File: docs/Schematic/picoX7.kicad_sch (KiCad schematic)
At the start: 33 parts, among them J1 MIDI in, J2 Debug, J3 Stereo line out, J4 Debug, SW1 RST, U1 MCU arm Cortex-M0x2, U2 I2S DAC, U3 H11L1, U4 74HCT164, U6 D1X8K-14BL, U7 D1X8K-14BL, U8 74HCT164

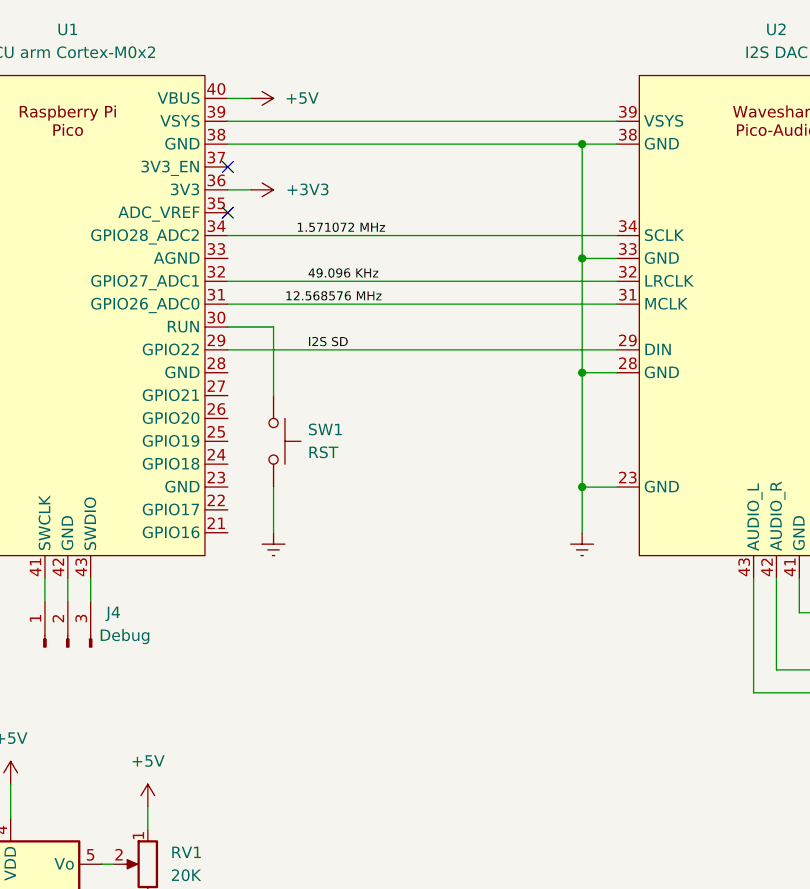
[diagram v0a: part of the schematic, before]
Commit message: Add ADC slider input
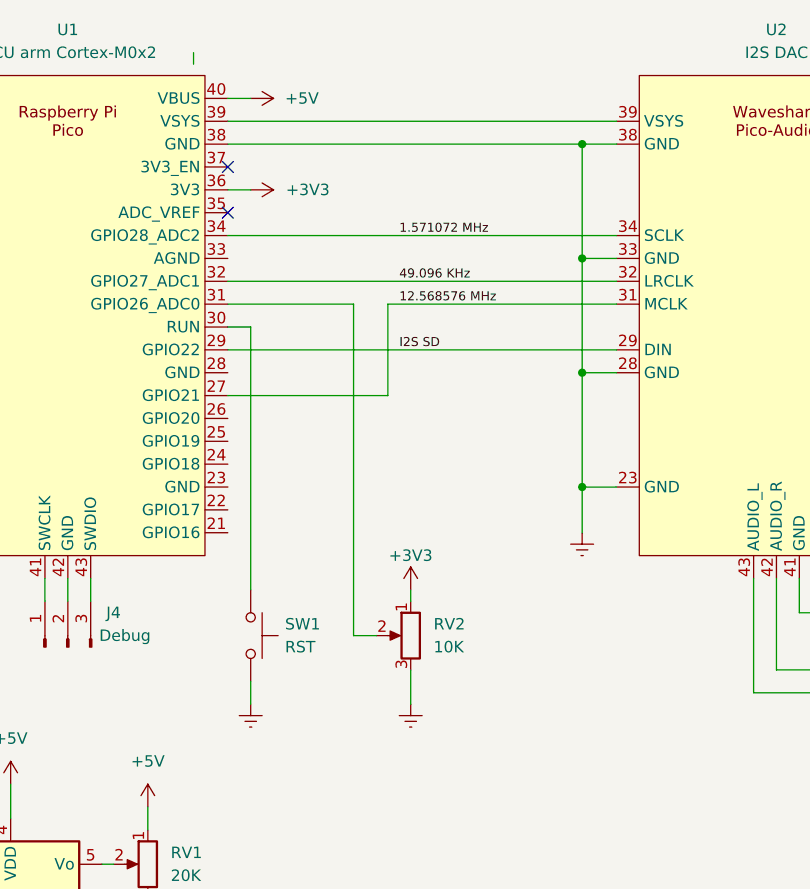
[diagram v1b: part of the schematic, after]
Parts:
- added RV2: 10K, symbol Device:R_Potentiometer
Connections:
- net +3V3: now also RV2.1
- net 12.568576 MHz: now also U1.27 (GPIO21); no longer U1.31 (GPIO26_ADC0)
- net Earth: now also RV2.3
- new net: RV2.2, U1.31 (GPIO26_ADC0)
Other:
- moved on the sheet: SW1

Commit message: Updated schematic
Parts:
- removed DS1: HY1602E, Display:HY1602E, symbol Display_Character:HY1602E
- removed RV1: 20K, symbol Device:R_Potentiometer
- removed RV2: 10K, symbol Device:R_Potentiometer
- removed U1: MCU arm Cortex-M0x2, Package_DIP:DIP-40_W25.4mm_Socket_LongPads, symbol MCU_RaspberryPi_and_Boards:Pico
- removed U2: I2S DAC, Package_DIP:DIP-40_W25.4mm_Socket_LongPads, symbol MCU_RaspberryPi_and_Boards:Waveshare Pico-Audio
- added C1, C3: 100nF, symbol Device:C
- added C2, C4: 47uF, symbol Device:C_Polarized
- added J5, J6: Stereo line out, Connector_Audio:Jack_3.5mm_CUI_SJ1-3523N_Horizontal, symbol Connector_Audio:AudioJack2_Ground
- added R19, R20: 220, Resistor_THT:R_Axial_DIN0204_L3.6mm_D1.6mm_P5.08mm_Horizontal, symbol Device:R
- added R21: 1.8K, Resistor_THT:R_Axial_DIN0204_L3.6mm_D1.6mm_P5.08mm_Horizontal, symbol Device:R
- added U1: Pico 2 (RP2350), RPi_Pico:RPi_Pico_SMD_TH, symbol MCU_RaspberryPi_and_Boards:Pico 2
- added U2: Pico-Audio, RPi_Pico:RPi_Pico_SMD_TH, symbol MCU_RaspberryPi_and_Boards:Pimoroni Pico-Audio
- added U5: Waveshare 16x2 I2C LCD (AIP31068L), RPi_Pico:RPi_Pico_SMD_TH, symbol MCU_RaspberryPi_and_Boards:Waveshare 16x2 I2C LCD
- added U9: Pico-Audio, RPi_Pico:RPi_Pico_SMD_TH, symbol MCU_RaspberryPi_and_Boards:Waveshare Pico-Audio
- R2: value 470 -> 1.8K
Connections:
- net +3V3: now also U1.36 (3V3), U5.1 (VCC)
- net +5V: now also U1.39 (VSYS), U1.40 (VBUS), U2.39 (VSYS), U9.39 (VSYS); no longer R2.1
- net Earth: now also R2.1, C1.2, C3.2, R21.1, U2.13 (GND), U2.18 (GND), U2.23 (GND), U2.28 (GND), U2.3 (GND), U2.33 (GND), U2.38 (GND), U2.8 (GND), U5.2 (GND), U9.13 (GND), U9.18 (GND), U9.23 (GND), U9.28 (GND), U9.3 (GND), U9.33 (GND), U9.38 (GND), U9.8 (GND)
- net I2S SD: now also U1.14 (GPIO10), U1.29 (GPIO22), U2.14 (SCLK), U9.29 (DIN)
- net console GND: now reaches J2.3 (Pin_3)
- net console GND: now also U1.3 (GND)
- net at SW1.1: now also U1.30 (RUN)
- net at U8.1 (DSA), U8.2 (DSB): now also U1.4 (GPIO2)
- net at U4.8 (CP), U8.8 (CP): now also U1.5 (GPIO3)
- net at J3.G: now also U2. (PHONES_OUT_R)
- net at J3.S: now also U2. (PHONES_OUT_R)
- net at J3.T: now also U2. (PHONES_OUT_R)
- net at R2.2: now also C2.2, J6.S
- net at J4.1 (Pin_1): now also U1.41 (SWCLK)
- net at J4.2 (Pin_2): now also U1.42 (GND)
- net at J4.3 (Pin_3): now also U1.43 (SWDIO)
- net 31250 baud 8-N-1 renamed MIDI 31250 baud 8-N-1
- net MIDI 31250 baud 8-N-1: now also U1.7 (GPIO5)
- net MIDI in (RX) 115200 baud 8-N-1 renamed console RX
- net console RX: now also U1.2 (GPIO1)
- net console (TX) 115200 baud 8-N-1 renamed console TX 115200 baud 8-N-1 
- net console TX 115200 baud 8-N-1 : now also U1.1 (GPIO0)
- new net: R20.2, U1.21 (GPIO16)
- new net: R19.2, U1.22 (GPIO17)
- new net: C1.1, C2.1, R19.1
- new net: C3.1, C4.1, R20.1
- new net: C4.2, J6.T, R21.2
- new net: J5.G, U9.41 (GND)
- new net: J5.S, U9.43 (AUDIO_L)
- new net: J5.T, U9.42 (AUDIO_R)
- new net I2C CLK: U1.20 (GPIO15), U5.3 (SCL)
- new net I2C SDA: U1.19 (GPIO14), U5.4 (SDA)
- new net I2S CLK 1.571072 MHz: U1.12 (GPIO9), U1.34 (GPIO28_ADC2), U2.12 (DIN), U9.34 (SCLK)
- new net I2S LR 49.096 KHz: U1.15 (GPIO11), U1.32 (GPIO27_ADC1), U2.15 (LRCLK), U9.32 (LRCLK)
- new net MCLK 12.568576 MHz: U1.31 (GPIO26_ADC0), U9.31 (MCLK)
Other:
- note added: "(1) Powered via micro USB connector on the Pico module (2) The line output is not stereo in the normal sense, 4 voices are on the left and 4 on the right and should be externally mixed for an 8 voice mono signal (3) The Pico's USB interface acts as a USB MIDI-IN when running (4) Raspberry Pi Pico-1 (RP2040) also supported"
- note added: "OPTIONAL I/O"
- note added: "PIMORONI Pico Audio I2S DAC"
- note added: "PWM DAC (ALTERNATIVE)"
- note added: "WAVESHARE I2S DAC (ALTERNATIVE)"
- note removed: "NOTE: Powered via micro USB connector on the Pico module"
- moved on the sheet: D1, J1, J2, J3, J4, R1, R10, R11, R12, R13, R14, R15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
